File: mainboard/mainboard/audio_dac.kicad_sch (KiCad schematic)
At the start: 10 parts, among them U4 TLV320DAC3203IRGET

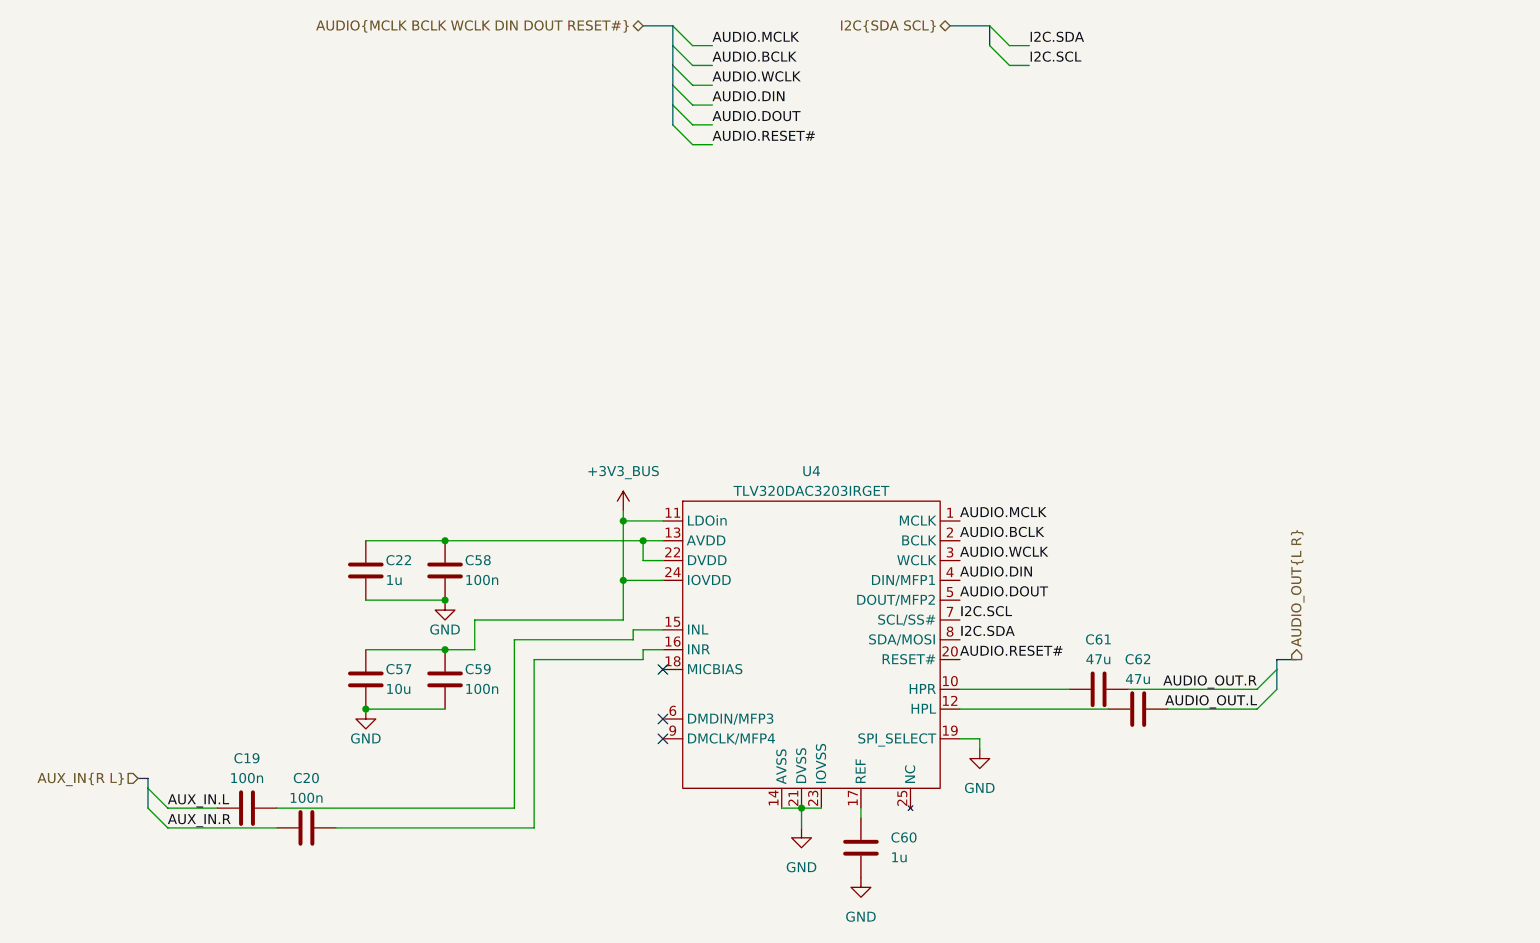
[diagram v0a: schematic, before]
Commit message: Share KiCad libraries, update v2.5 mainboard schematics
- Move every board's symbols, footprints and 3D models into libs/ and point
  the projects' lib tables there; add the mspc design-block library.
- Mainboard: new debug probe, MSPC bus and power connector sheets; drop the
  old shared-bus, south/north bridge and SD card sheets.
- Remove orphaned sheets from the GPU cards and the simulation sandbox.
- Rewrite the v2.5 plan, document libs/ in the README, ignore KiCad 10
  restore backups.

Co-Authored-By: Claude Opus 5 (1M context) <noreply@anthropic.com>
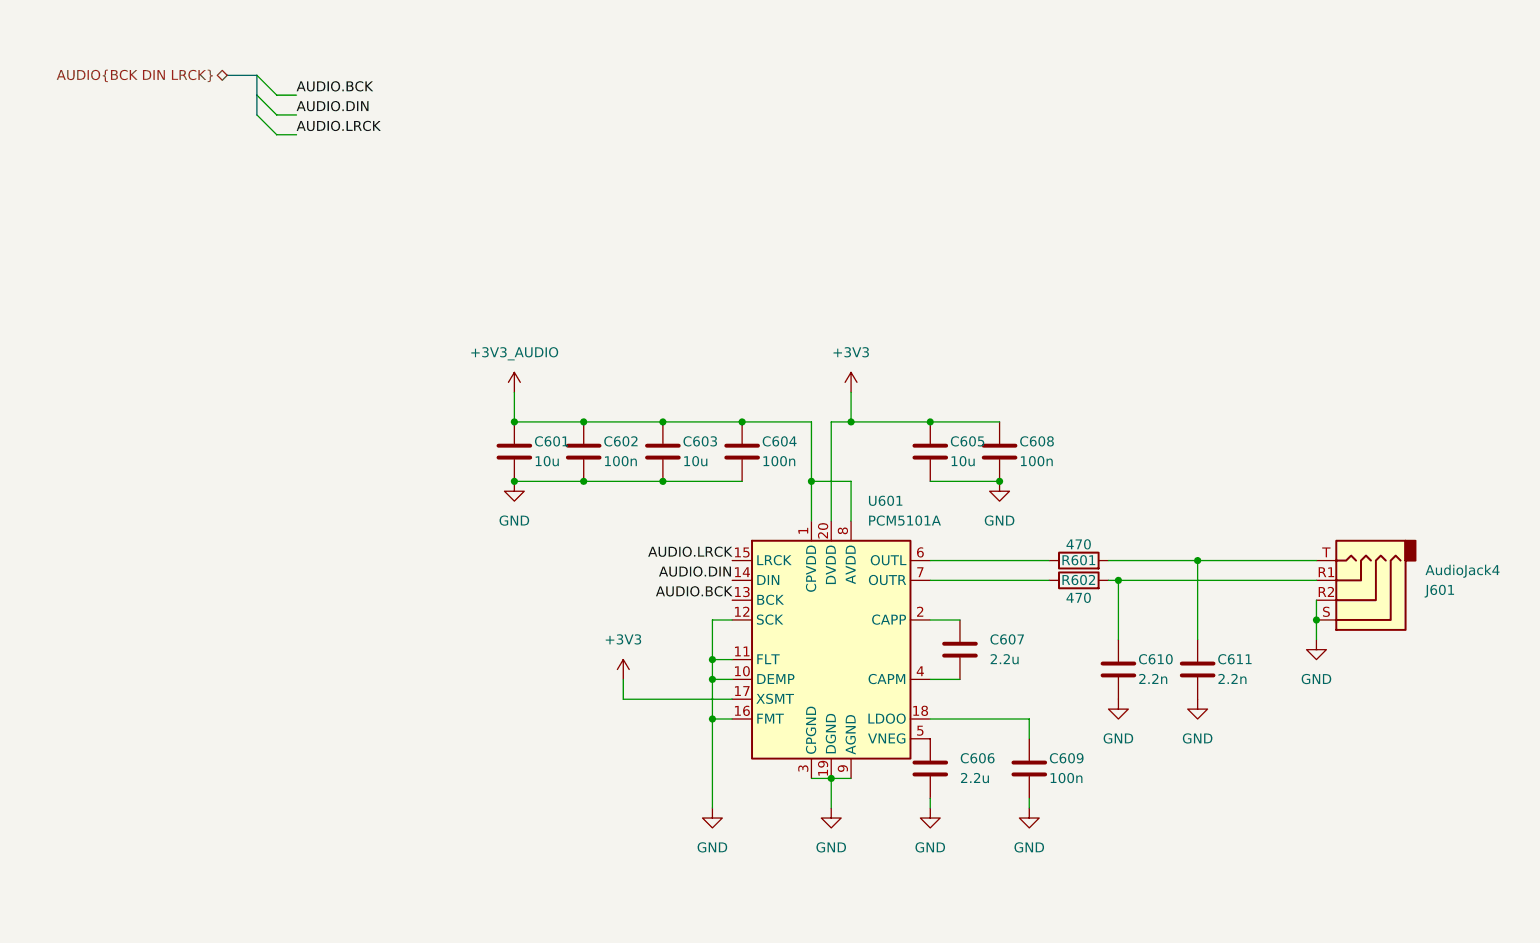
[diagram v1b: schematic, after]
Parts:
- removed C19, C20, C58, C59: 100n, Capacitor_SMD:C_0402_1005Metric_Pad0.74x0.62mm_HandSolder, symbol Device:C
- removed C22, C60: 1u, Capacitor_SMD:C_0402_1005Metric_Pad0.74x0.62mm_HandSolder, symbol Device:C
- removed C57: 10u, Capacitor_SMD:C_1206_3216Metric_Pad1.33x1.80mm_HandSolder, symbol Device:C
- removed C61, C62: 47u, Capacitor_SMD:C_1206_3216Metric_Pad1.33x1.80mm_HandSolder, symbol Device:C
- removed U4: TLV320DAC3203IRGET, Package_DFN_QFN:VQFN-24-1EP_4x4mm_P0.5mm_EP2.45x2.45mm, symbol Project Audio DAC:TLV320DAC3203IRGET
- added C601, C603, C605: 10u, Capacitor_SMD:C_1206_3216Metric_Pad1.33x1.80mm_HandSolder, symbol Device:C
- added C602, C604, C608, C609: 100n, Capacitor_SMD:C_0402_1005Metric_Pad0.74x0.62mm_HandSolder, symbol Device:C
- added C606, C607: 2.2u, Capacitor_SMD:C_0603_1608Metric_Pad1.08x0.95mm_HandSolder, symbol Device:C
- added C610, C611: 2.2n, Capacitor_SMD:C_0402_1005Metric_Pad0.74x0.62mm_HandSolder, symbol Device:C
- added J601: AudioJack4, Connector_Audio:Jack_3.5mm_PJ320D_Horizontal, symbol Connector:AudioJack4
- added R601, R602: 470, Resistor_SMD:R_0402_1005Metric_Pad0.72x0.64mm_HandSolder, symbol Device:R
- added U601: PCM5101A, Package_SO:TSSOP-20_4.4x6.5mm_P0.65mm, symbol Audio:PCM5101A
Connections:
- net AUDIO.DIN: now also U601.14 (DIN)
- net GND: now also C601.2, C602.2, C603.2, C604.2, C605.2, C606.2, C608.2, C609.2, C610.2, C611.2, J601.R2, J601.S, U601.10 (DEMP), U601.11 (FLT), U601.12 (SCK), U601.16 (FMT), U601.19 (DGND), U601.3 (CPGND), U601.9 (AGND)
- new net: C610.1, J601.R1, R602.2
- new net: C611.1, J601.T, R601.2
- new net: R602.1, U601.7 (OUTR)
- new net: C606.1, U601.5 (VNEG)
- new net: C609.1, U601.18 (LDOO)
- new net: C607.1, U601.2 (CAPP)
- new net: C607.2, U601.4 (CAPM)
- new net: R601.1, U601.6 (OUTL)
- new net +3V3: C605.1, C608.1, U601.17 (XSMT), U601.20 (DVDD)
- new net +3V3_AUDIO: C601.1, C602.1, C603.1, C604.1, U601.1 (CPVDD), U601.8 (AVDD)
- new net AUDIO.BCK: U601.13 (BCK)
- new net AUDIO.LRCK: U601.15 (LRCK)
- no-connect marks 3 -> 0

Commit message: Mainboard v3: schematic review fixes
New sheets for the housekeeping bus: TCA6408A expander, INA226/INA3221
power measurement and the MCP7940N RTC with a CR1220 backup cell.

Correctness:
- RTC load caps C241/C242 are 6.8 pF C0G 0402 (were a relay footprint).
- L50 is the AOTA-B201610S3R3-101-T with pin 1 on +1V1_MCU; U52 is an
  APS1604M-3SQR-SN on a 150-mil SOP-8.
- I2S is DIN=GPIO13, BCK=GPIO14, LRCK=GPIO15, as pico-extras audio_i2s
  expects. Expander INT# goes to GPIO42.
- ADC_AVDD filter (FB50, C74, C75), 33 ohm on SDIO CLK, SD ESD (U53/U54),
  PSRAM 1 uF, POWER_BUTTON 10 k pull-up, 10 uF at the SY6280 inputs.
- J_DBG: USBLC6-4SC6 on the probe USB, 47 uF polymer on +5V_DBG against
  charger overvoltage spikes, and bleeders on both USB-C VBUS inputs and
  on +5V_DBG.
- Power symbols point at their matching project_power symbols.

Parts and fields:
- Part numbers and LCSC codes for the purchased parts: push-push microSD
  J53, HRO USB-C J1/J2, stacked USB-A J90/J91, TLV70033DDCR, and others.
- Voltage, dielectric and tolerance fields on every capacitor and a
  tolerance on every resistor; the field is named "LCSC" everywhere.
- Hand-solder footprint variants where KiCad has one.

Drawing:
- References renumbered into the per-sheet ranges.
- Net names on the USB, crystal, DAC, CC and ISET nets; netclass
  patterns updated.
- No four-way junctions left.
- Notes for the slot pin 1 marking, J120 and firmware bring-up.

ERC is clean with all rules enabled.

Co-Authored-By: Claude Opus 5 (1M context) <noreply@anthropic.com>
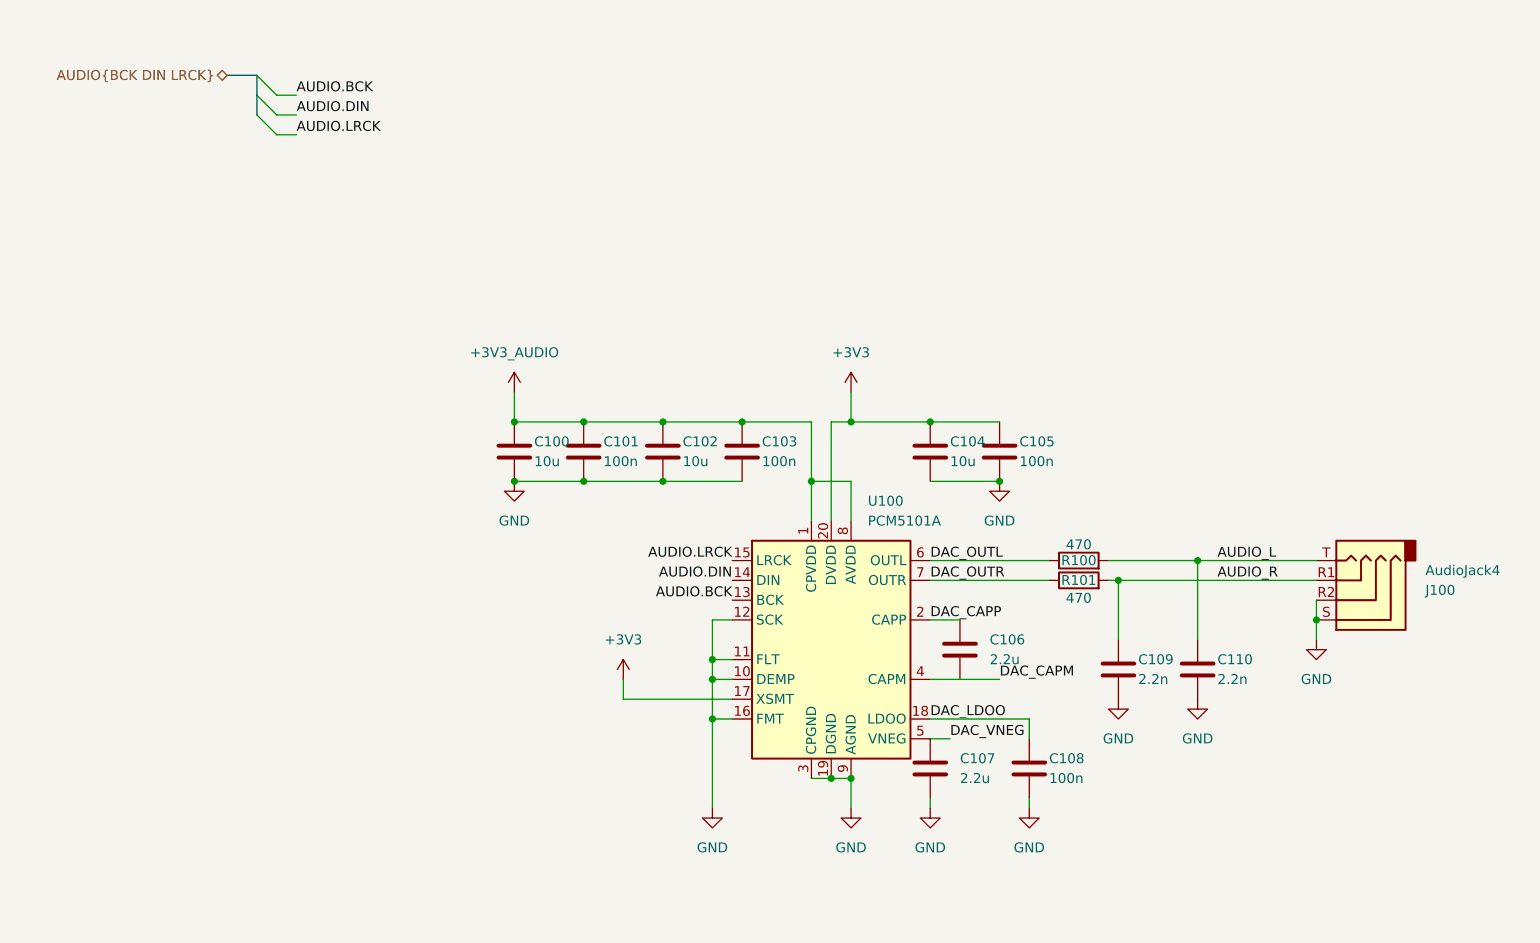
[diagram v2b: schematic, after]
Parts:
- C100: renamed from C601; Dielectric (none) -> X5R; LCSC (none) -> C9807; MPN (none) -> CL31A106KAHNNNE; Tolerance (none) -> 10%; Voltage (none) -> 25V
- C101: renamed from C602; Dielectric (none) -> X7R; Tolerance (none) -> 10%; Voltage (none) -> 16V
- C102: renamed from C603; Dielectric (none) -> X5R; LCSC (none) -> C9807; MPN (none) -> CL31A106KAHNNNE; Tolerance (none) -> 10%; Voltage (none) -> 25V
- C103: renamed from C604; Dielectric (none) -> X7R; Tolerance (none) -> 10%; Voltage (none) -> 16V
- C104: renamed from C605; Dielectric (none) -> X5R; LCSC (none) -> C9807; MPN (none) -> CL31A106KAHNNNE; Tolerance (none) -> 10%; Voltage (none) -> 25V
- C105: renamed from C608; Dielectric (none) -> X7R; Tolerance (none) -> 10%; Voltage (none) -> 16V
- C106: renamed from C607; Dielectric (none) -> X5R; Tolerance (none) -> 10%; Voltage (none) -> 10V
- C107: renamed from C606; Dielectric (none) -> X5R; Tolerance (none) -> 10%; Voltage (none) -> 10V
- C108: renamed from C609; Dielectric (none) -> X7R; Tolerance (none) -> 10%; Voltage (none) -> 16V
- C109: renamed from C610; Dielectric (none) -> C0G; Tolerance (none) -> 5%; Voltage (none) -> 10V
- C110: renamed from C611; Dielectric (none) -> C0G; Tolerance (none) -> 5%; Voltage (none) -> 10V
- J100: renamed from J601; symbol Connector:AudioJack4 -> Connector_Audio:AudioJack4
- R100: renamed from R601; Tolerance (none) -> 1%
- R101: renamed from R602; Tolerance (none) -> 1%
- U100: renamed from U601; LCSC (none) -> C2667024; MPN (none) -> PCM5101APWR; Manufacturer (none) -> Texas Instruments
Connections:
- net AUDIO_R: now reaches C109.1, J100.R1, R101.2
- net AUDIO_L: now reaches C110.1, J100.T, R100.2
- net DAC_OUTR: now reaches R101.1, U100.7 (OUTR)
- net DAC_VNEG: now reaches C107.1, U100.5 (VNEG)
- net DAC_LDOO: now reaches C108.1, U100.18 (LDOO)
- net DAC_CAPP: now reaches C106.1, U100.2 (CAPP)
- net DAC_CAPM: now reaches C106.2, U100.4 (CAPM)
- net DAC_OUTL: now reaches R100.1, U100.6 (OUTL)

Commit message: Mainboard: title blocks for v3
Every schematic sheet and the PCB carry the same title block: "MSPC
mainboard", rev 3, 2026-09-13. The root sheet still said rev 1 from
2022, and most sheets had none.

Co-Authored-By: Claude Opus 5 (1M context) <noreply@anthropic.com>
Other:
- company: (none) -> Mateusz Stadnik
- title: (none) -> MSPC mainboard
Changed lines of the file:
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@@
 	(generator_version "10.0")
 	(paper "A4")
+	(title_block
+		(title "MSPC mainboard")
+		(date "2026-09-13")
+		(rev "3")
+		(company "Mateusz Stadnik")
+	)
 	(junction
 		(at 101.6 76.2)
